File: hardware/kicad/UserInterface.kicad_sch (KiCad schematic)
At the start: 0 parts

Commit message: usb interface
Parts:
- added C19: 100nF, symbol Device:C
- added D11: INS/LINE_IND, Diode_THT:D_DO-35_SOD27_P7.62mm_Horizontal, symbol Device:LED
- added R26: 1K, Package_TO_SOT_SMD:SOT-23, symbol Device:R
- added SW1: HIZ_SW, Button_Switch_THT:SW_NKK_GW12LJP, symbol Switch:SW_Push
- added SW2: 48V_SW, Button_Switch_THT:SW_NKK_GW12LJP, symbol Switch:SW_Push
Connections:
- new net: D11.2 (A), R26.2
- new net +5V: SW1.2
- new net GND: C19.2, D11.1 (K)
- new net HIZ_FET_GATE: C19.1, R26.1, SW1.1
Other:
- note added: "INST/LINE Latching Button"
- note added: "Phantom Power Latching Button"

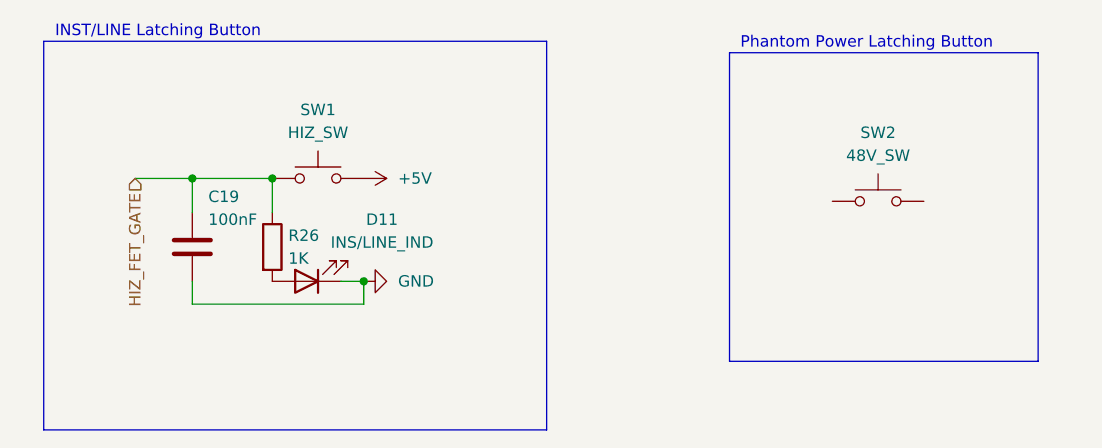
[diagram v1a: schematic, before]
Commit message: add phtm indicator and mcu sheet
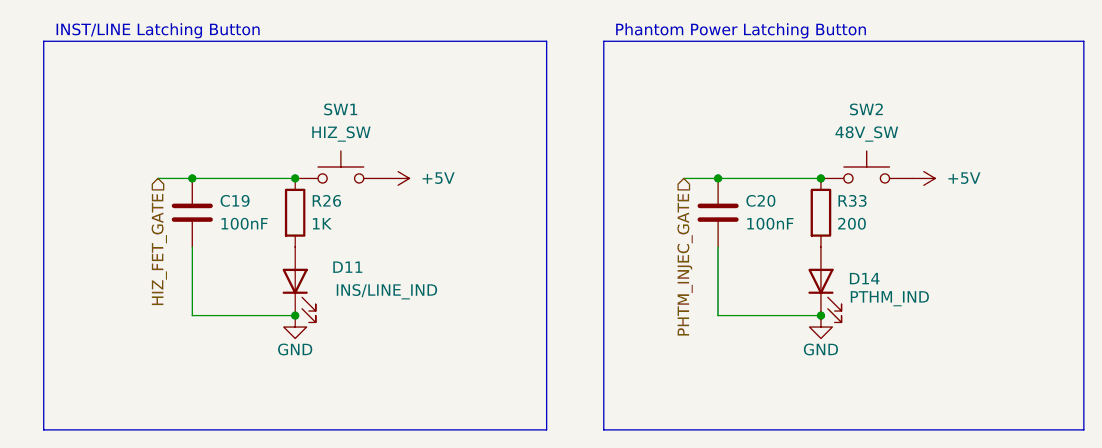
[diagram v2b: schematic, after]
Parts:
- added C20: 100nF, symbol Device:C
- added D14: PTHM_IND, Diode_THT:D_DO-35_SOD27_P7.62mm_Horizontal, symbol Device:LED
- added R33: 200, Package_TO_SOT_SMD:SOT-23, symbol Device:R
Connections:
- net +5V: now also SW2.2
- net GND: now also C20.2, D14.1 (K)
- net PHTM_INJEC_GATE: now reaches SW2.1
- net PHTM_INJEC_GATE: now also C20.1, R33.1
- new net: D14.2 (A), R33.2
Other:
- moved on the sheet: C19, D11, R26, SW1, SW2
